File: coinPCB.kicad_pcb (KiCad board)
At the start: 2 copper layers, 50.8 x 50.8 mm, 12 parts, among them P1 CONN_01X08, P2 CONN_01X08, Q1 2N2222A, U1 TSOP38238, U2 DHT12

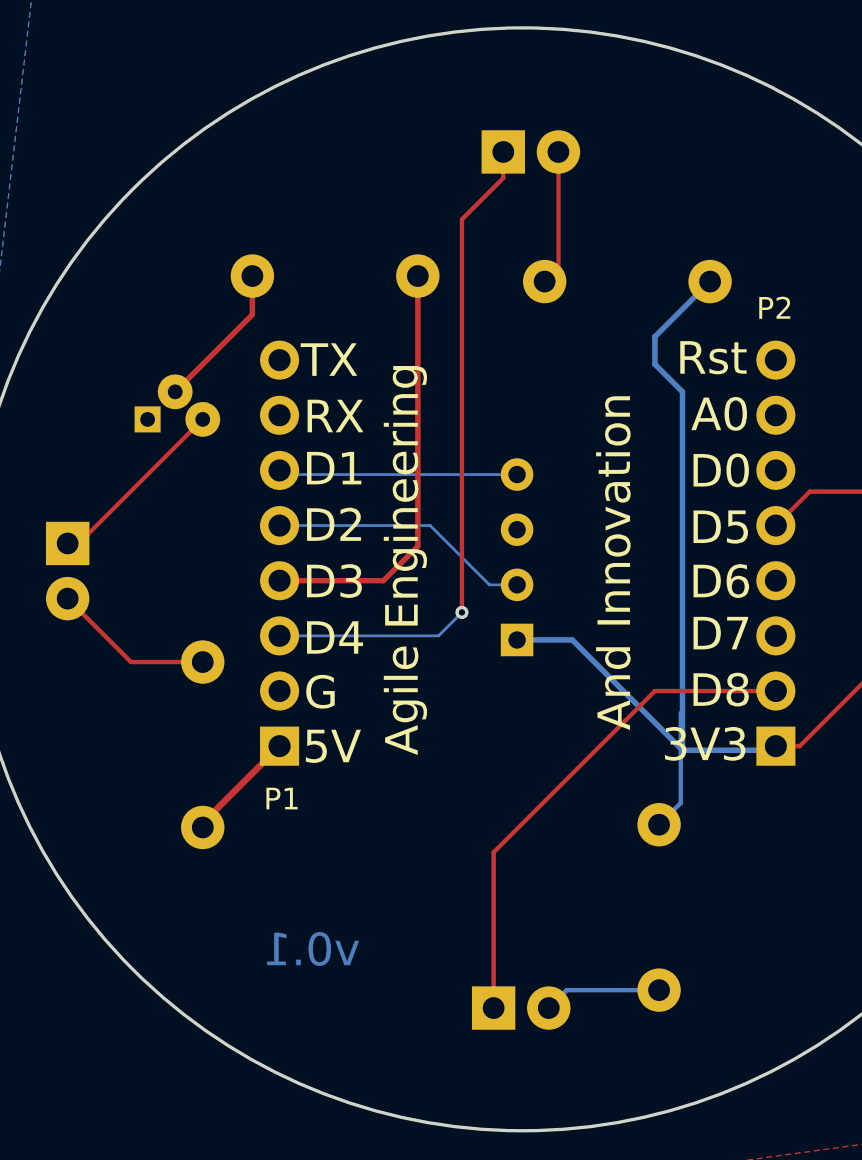
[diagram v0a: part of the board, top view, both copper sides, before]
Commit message: fixed all errors and should build correctly
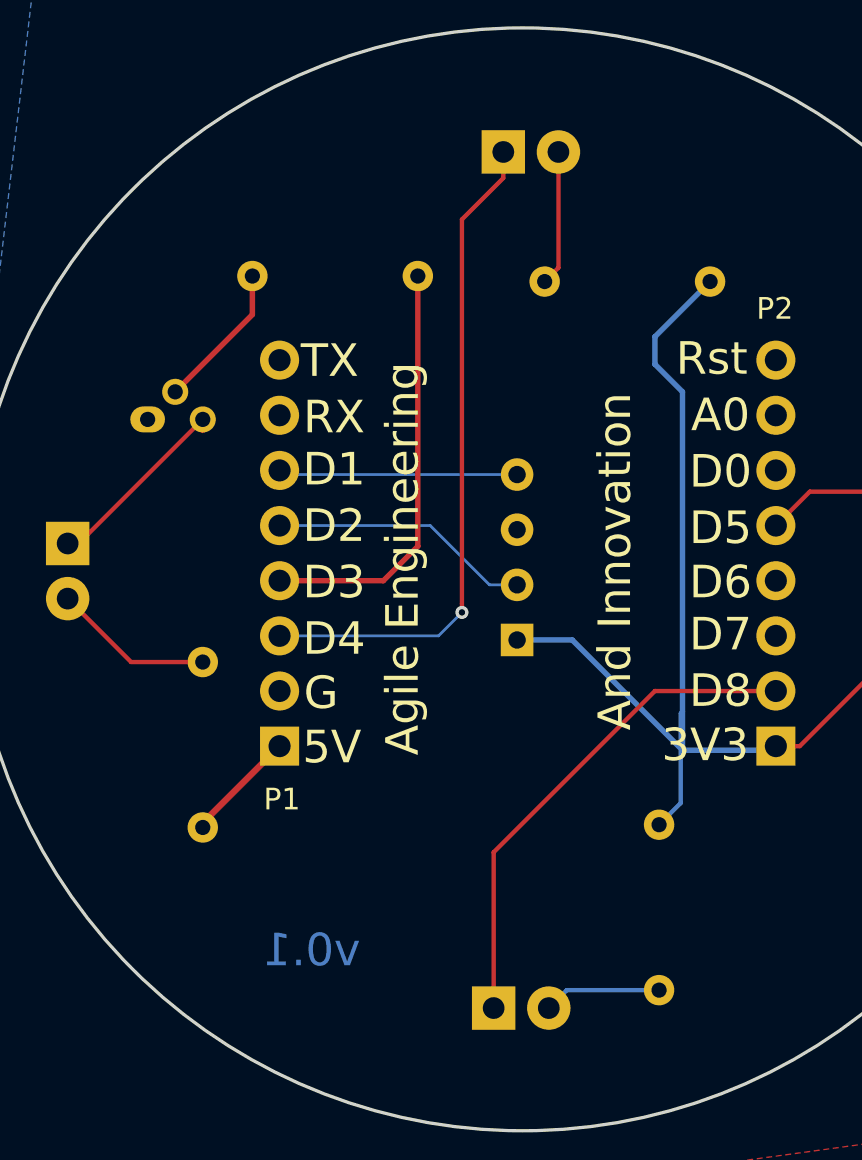
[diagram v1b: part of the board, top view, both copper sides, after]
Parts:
- D2, D3: footprint LEDs:LED-3MM -> digikey-footprints:LED_3mm_Radial
- Q1: footprint digikey-footprints:TO-18-3 -> Package_TO_SOT_THT:TO-18-3
- R1, R2, R3, R4: footprint Resistors_ThroughHole:Resistor_Horizontal_RM7mm -> Resistor_THT:R_Axial_DIN0204_L3.6mm_D1.6mm_P7.62mm_Horizontal
- moved D3 2.54 mm to (140.3, 76.6)
- moved D2 2.54 mm to (139.9, 116.0)

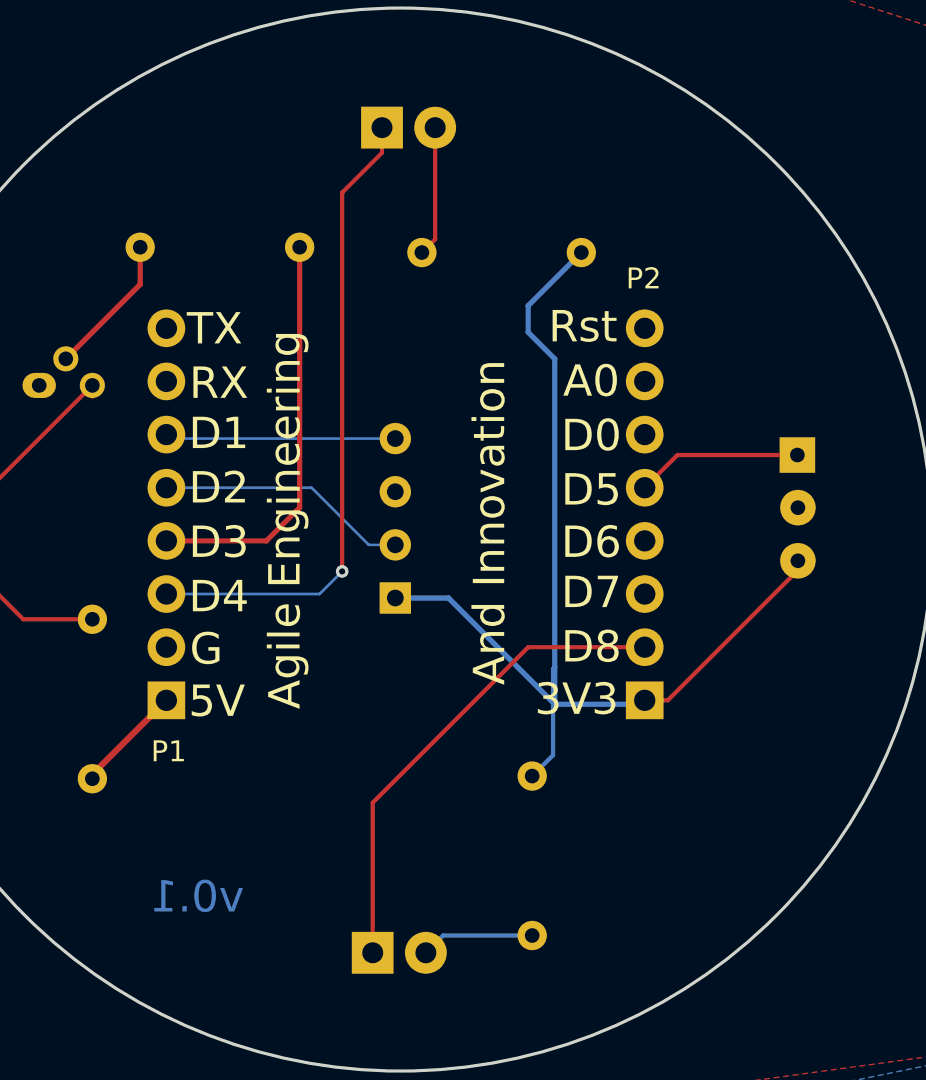
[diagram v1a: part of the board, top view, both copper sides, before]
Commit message: fixed schematic errors, including taking out 1k resitor from D3 because that pin as pull-up resistor arleady, and running D4 and D8 to ground
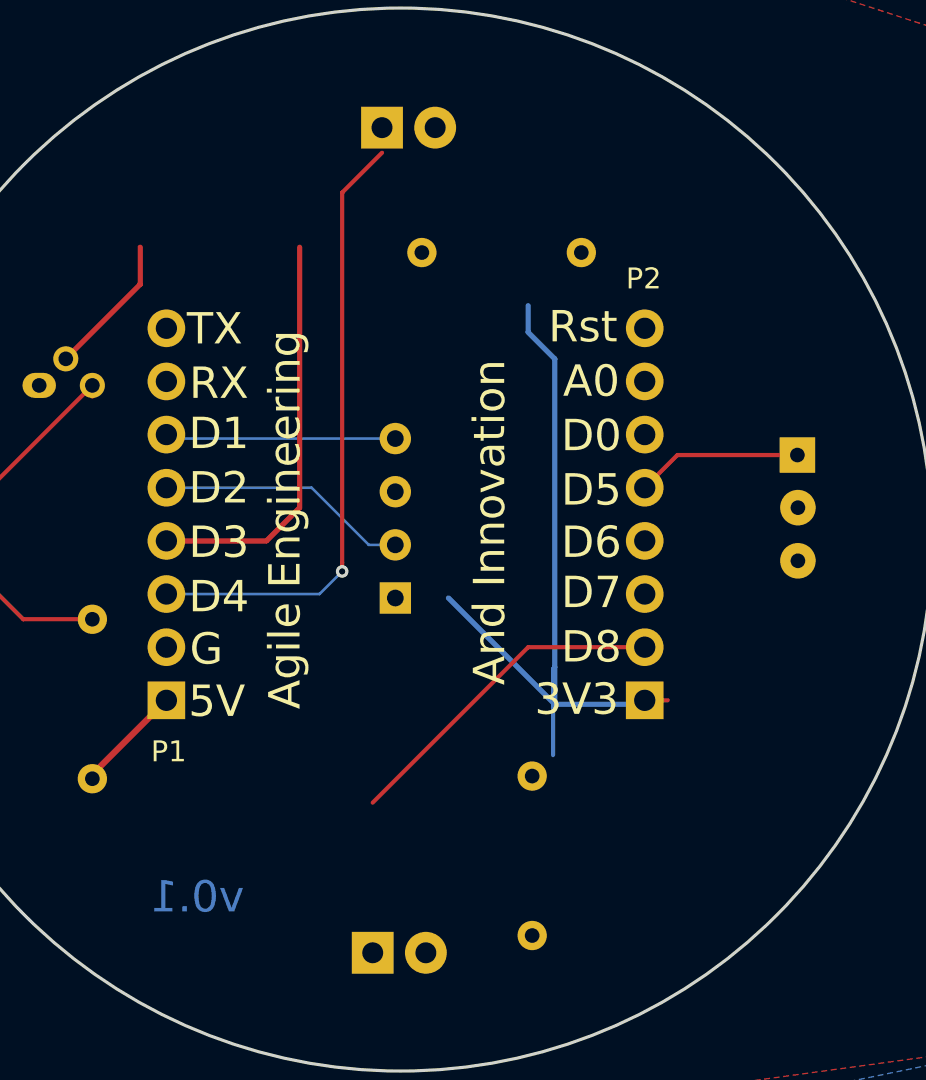
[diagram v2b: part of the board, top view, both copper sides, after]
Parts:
- removed R1: 1K, Resistor_THT:R_Axial_DIN0204_L3.6mm_D1.6mm_P7.62mm_Horizontal
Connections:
- net /+5V renamed +5V
- D2 pad 1: /D8 -> Net-(D2-Pad1)
- D2 pad 2: Net-(D2-Pad2) -> /D8
- D3 pad 1: /D4 -> Net-(D3-Pad1)
- D3 pad 2: Net-(D3-Pad2) -> /D4
- Q1 pad 2: Net-(Q1-Pad2) -> /D3
- R3 pad 1: VCC -> Net-(D2-Pad1)
- R3 pad 2: Net-(D2-Pad2) -> GND
- R4 pad 1: VCC -> Net-(D3-Pad1)
- R4 pad 2: Net-(D3-Pad2) -> GND
- U1 pad 3: VCC -> +3V3
- U2 pad 1: VCC -> +3V3
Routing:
- net VCC: track 53.3 -> 36.5 mm
- net /D8: track 23.3 -> 16.1 mm
- net Net-(Q1-Pad2): track 6.81 -> 0.00 mm
- net /D3: track 19.5 -> 26.3 mm
- net Net-(D3-Pad2): track 6.23 -> 0.00 mm
- net Net-(D2-Pad2): track 5.42 -> 0.00 mm
- net /D4: track 30.8 -> 29.6 mm

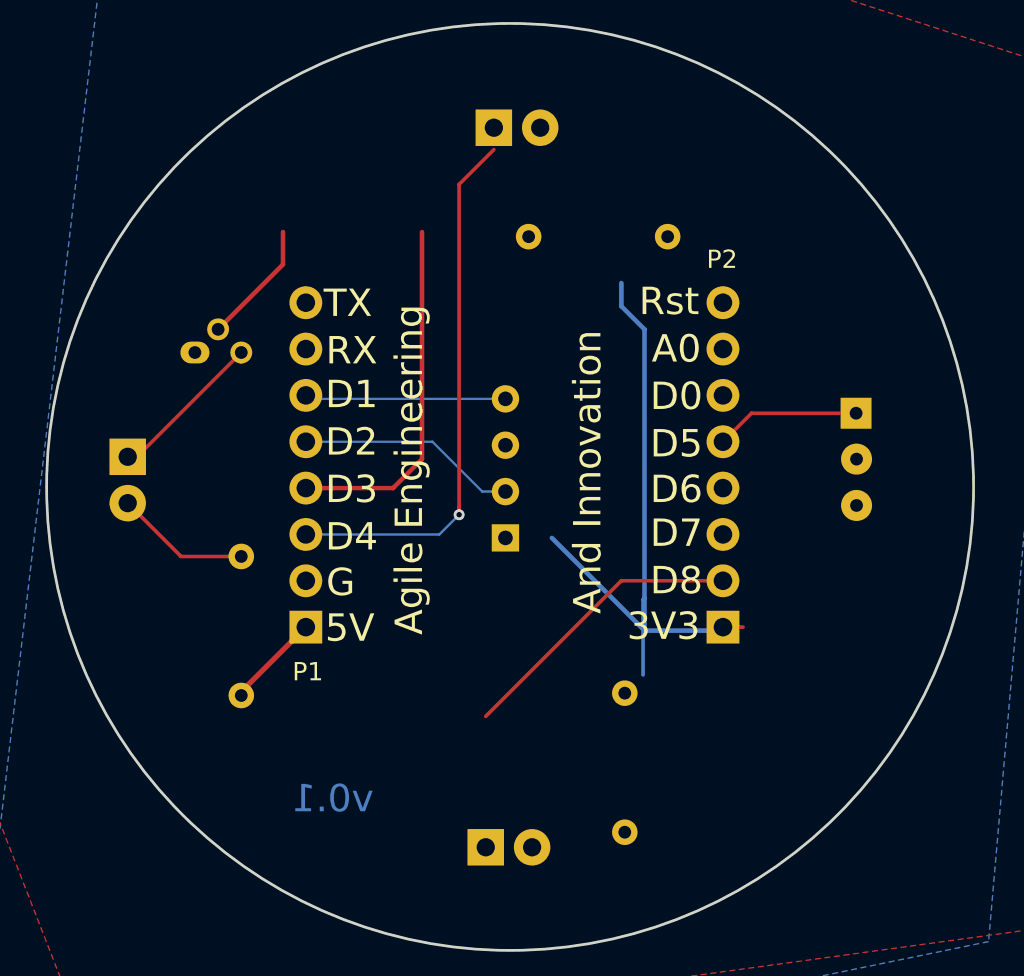
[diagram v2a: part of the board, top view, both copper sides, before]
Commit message: began laying out v0.2 with digikeyfootprins
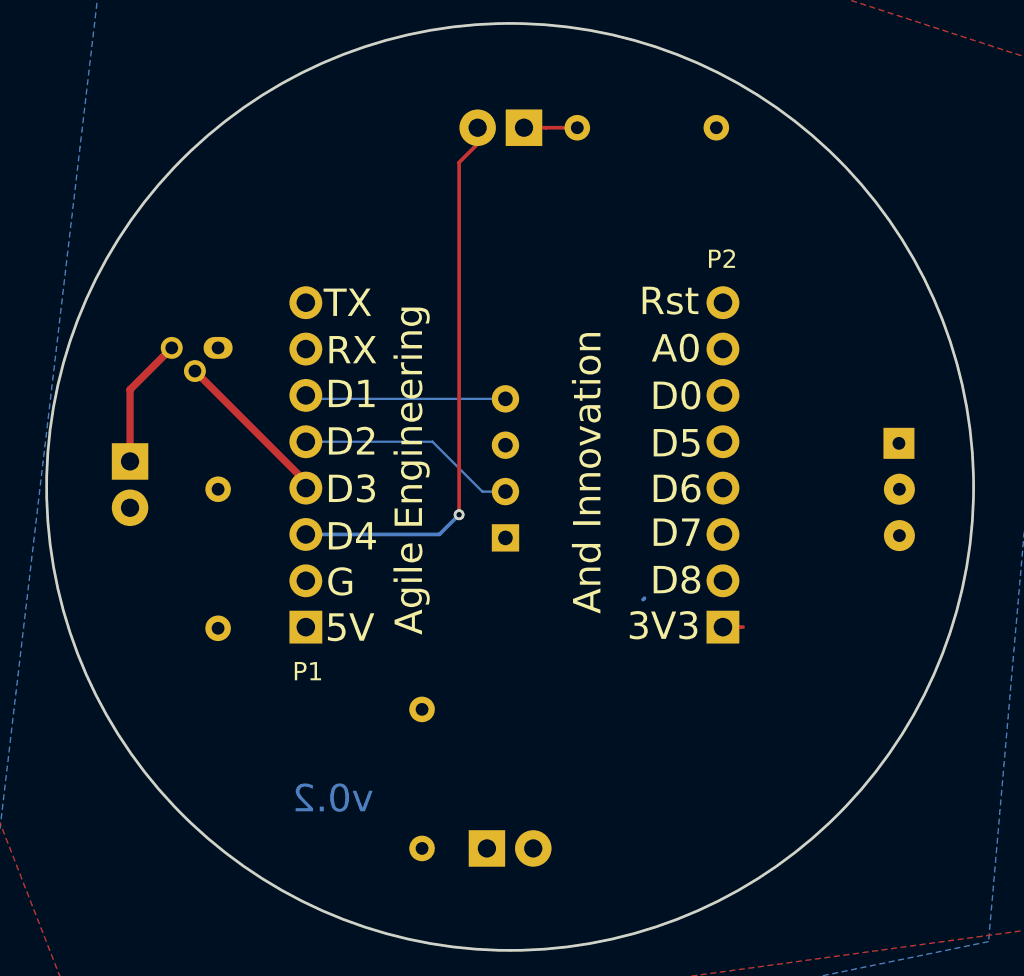
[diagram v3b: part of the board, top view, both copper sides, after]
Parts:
- removed D1, D2, D3: LED, digikey-footprints:LED_3mm_Radial
- removed R4: 100, Resistor_THT:R_Axial_DIN0204_L3.6mm_D1.6mm_P7.62mm_Horizontal
- added D10: LED, digikey-footprints:LED_3mm_Radial, B.Cu at (140.0, 116.1)
- added D11: LED, digikey-footprints:LED_3mm_Radial, B.Cu at (136.9, 76.6)
- added D9: LED, digikey-footprints:LED_3mm_Radial, B.Cu at (117.9, 97.4)
- added R1: 100, Resistor_THT:R_Axial_DIN0204_L3.6mm_D1.6mm_P7.62mm_Horizontal, B.Cu at (122.7, 104.0)
- moved R3 31.1 mm to (142.4, 76.6), turned to 0 degrees
- moved R2 13.0 mm to (133.9, 116.1)
- moved U1 2.87 mm to (160.0, 93.9)
- moved Q1 1.30 mm to (122.7, 88.6), turned to 180 degrees
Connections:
- P1 pad 7: /RX -> (no net)
- P1 pad 8: /TX -> (no net)
- P2 pad 1: VCC -> (no net)
- P2 pad 3: /D7 -> (no net)
- P2 pad 4: /D6 -> (no net)
- P2 pad 6: /D0 -> (no net)
- P2 pad 7: /A0 -> (no net)
- P2 pad 8: /RST -> (no net)
- R2 pad 1: +5V -> Net-(D10-Pad1)
- R2 pad 2: Net-(D1-Pad2) -> GND
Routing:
- net VCC: track 36.5 -> 0.00 mm
- net /D3: track 26.3 -> 8.93 mm
- net /D8: track 16.1 -> 0.00 mm
- net /D5: track 7.94 -> 0.00 mm
- net Net-(D1-Pad2): track 7.43 -> 0.00 mm
- net +5V: track 5.21 -> 0.00 mm
- net Net-(D11-Pad1): track 0.00 -> 2.92 mm
- net (no net): track 0.00 -> 1.48 mm
- net Net-(D9-Pad1): track 9.10 -> 7.68 mm
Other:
- board text added: "v0.2"
- board text removed: "v0.1"

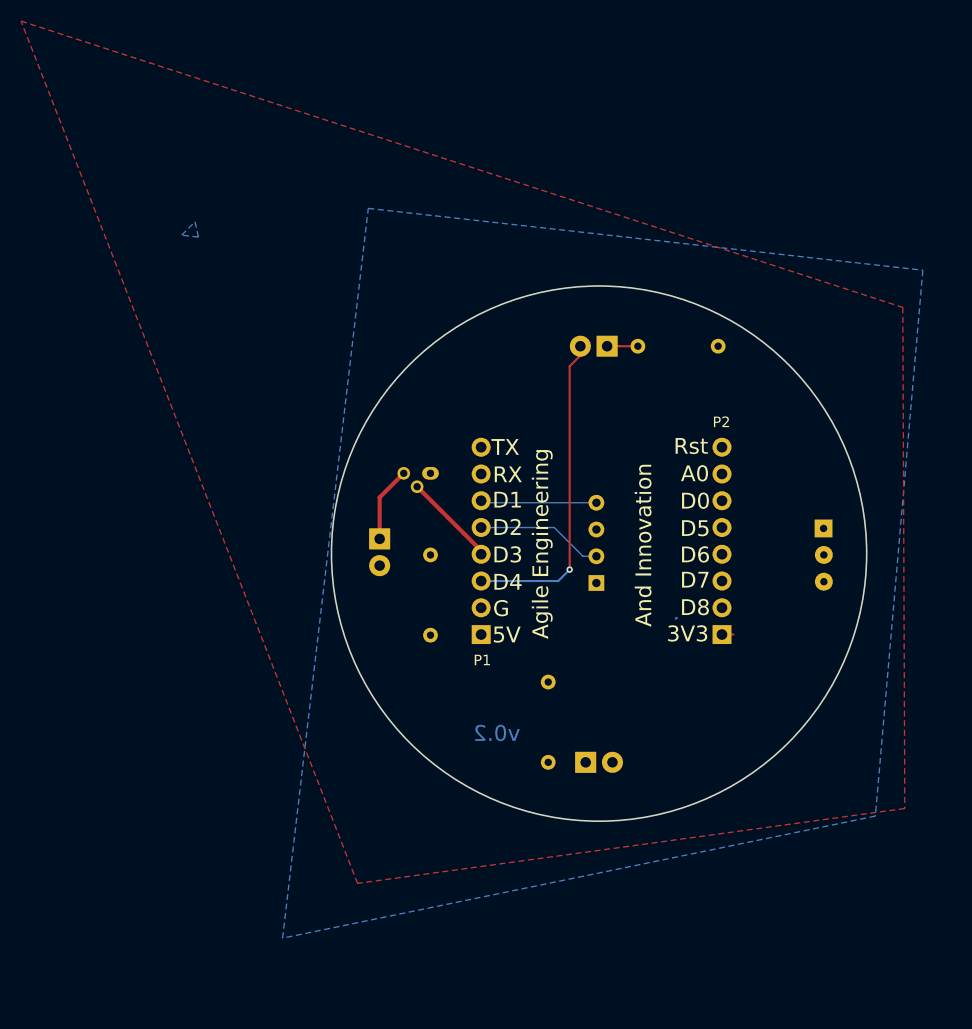
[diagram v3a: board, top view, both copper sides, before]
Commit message: finished initial PCB trace layout and added the copper backplane as well as fixed the digi-key model of the IR_LED_TSAL_6100 to have the Cathode be the square pad.
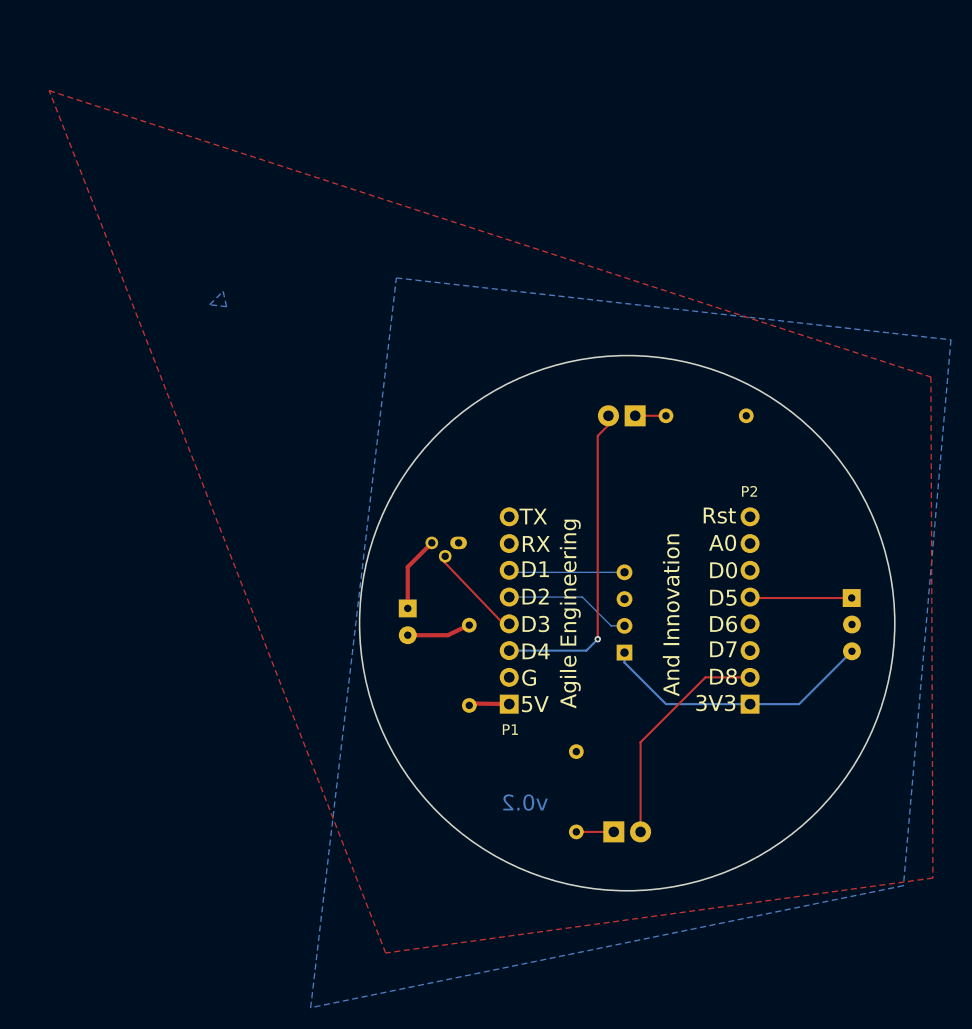
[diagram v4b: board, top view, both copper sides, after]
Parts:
- D9: footprint digikey-footprints:LED_3mm_Radial -> digikey-footprints:LED_IR_TSAL6100
- moved R1 7.62 mm to (126.4, 110.7)
- moved P1 7.12 mm to (130.2, 110.6)
- moved D10 7.12 mm to (142.6, 122.7)
- moved D11 7.12 mm to (139.6, 83.2)
- moved D9 7.12 mm to (120.5, 104.0), turned to 90 degrees
- moved P2 7.12 mm to (153.0, 110.6)
- moved Q1 7.12 mm to (125.3, 95.2)
- moved R2 7.12 mm to (136.5, 122.7)
- moved R3 7.12 mm to (145.0, 83.2)
- moved U1 7.12 mm to (162.7, 100.5)
- moved U2 7.12 mm to (141.1, 105.7)
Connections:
- P1 pad 7: (no net) -> /RX
- P1 pad 8: (no net) -> /TX
- P2 pad 1: (no net) -> +3V3
- P2 pad 3: (no net) -> /D7
- P2 pad 4: (no net) -> /D6
- P2 pad 6: (no net) -> /D0
- P2 pad 7: (no net) -> /A0
- P2 pad 8: (no net) -> /RST
- Q1 pad 3: Net-(D9-Pad1) -> Net-(D9-Pad2)
- R1 pad 2: Net-(D9-Pad2) -> Net-(D9-Pad1)
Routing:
- net +3V3: track 0.00 -> 27.4 mm
- net /D8: track 0.00 -> 21.5 mm
- net /D5: track 0.00 -> 9.68 mm
- net Net-(D9-Pad2): track 0.00 -> 7.68 mm
- net +5V: track 0.00 -> 3.79 mm
- net Net-(D10-Pad1): track 0.00 -> 3.56 mm
- net Net-(D9-Pad1): track 7.68 -> 5.85 mm
- net (no net): track 1.48 -> 0.00 mm
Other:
- board text added: "K"
